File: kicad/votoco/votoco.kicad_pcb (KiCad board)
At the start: 4 copper layers, 64 x 36.5 mm, 98 parts, among them J1 Conn_01x02, J10 Conn_01x02, J11 Conn_01x02, J12 Conn_01x02, J13 Conn_01x02, J14 Conn_01x02, J2 Conn_01x04, J3 Conn_02x05_Odd_Even, J4 Conn_01x03, J5 Conn_01x02, J6 Conn_01x02, J7 Conn_01x02, J8 Conn_01x03, J9 USB_B_Micro, Q1 RQ6E045TN, Q2 RQ6E045TN, Q3 RQ6E045TN, SW1 Reset, SW2 Boot, U1 SN65HVD231, U2 TMC2209-LA-T, U3 STM32F042G6Ux, U4 74AHC1G08, U5 MAX2040xAFL, U6 NCP1117-3.3, U7 ADXL345BCCZ, Y1 12Mhz

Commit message: some error from V1.0 corrected
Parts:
- added R23: 20k, Resistor_SMD:R_0603_1608Metric, B.Cu at (133.9, 85.1)
- C16: value 10µ 50V -> 100µ 35V; footprint Capacitor_SMD:CP_Elec_4x3 -> Capacitor_SMD:CP_Elec_6.3x7.7
- U2: value TMC2209-LA-T -> QFN28_5X5_3X8_EPAD_TRI
- moved C16 6.21 mm to (139.8, 85.5), turned to 180 degrees
- moved R10 5.25 mm to (133.9, 88.2), turned to 90 degrees
- moved R9 3.51 mm to (132.2, 88.2), turned to -90 degrees
- moved C15 3.45 mm to (139.6, 89.8), turned to 180 degrees
- moved C13 0.10 mm to (142.7, 89.8)
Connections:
- R4 pad 1: GND -> +3V3
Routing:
- net GND: track 82.5 -> 88.7 mm, vias 62 -> 66
- net +24V: track 57.7 -> 62.9 mm, vias 34 -> 37
- net Net-(R10-Pad1): track 4.67 -> 6.94 mm
- net Net-(C3-Pad2): track 18.3 -> 16.1 mm
- net ENN: track 41.6 -> 43.6 mm
- net +3V3: track 42.5 -> 44.0 mm, vias 23 -> 25
- net SWCLK: track 46.6 -> 46.0 mm
- net DIR: track 24.3 -> 23.6 mm
- net SWDIO/DI2: track 86.1 -> 85.5 mm
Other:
- board text added: "Votoco 1.1"
- board text removed: "Votoco 1.0"

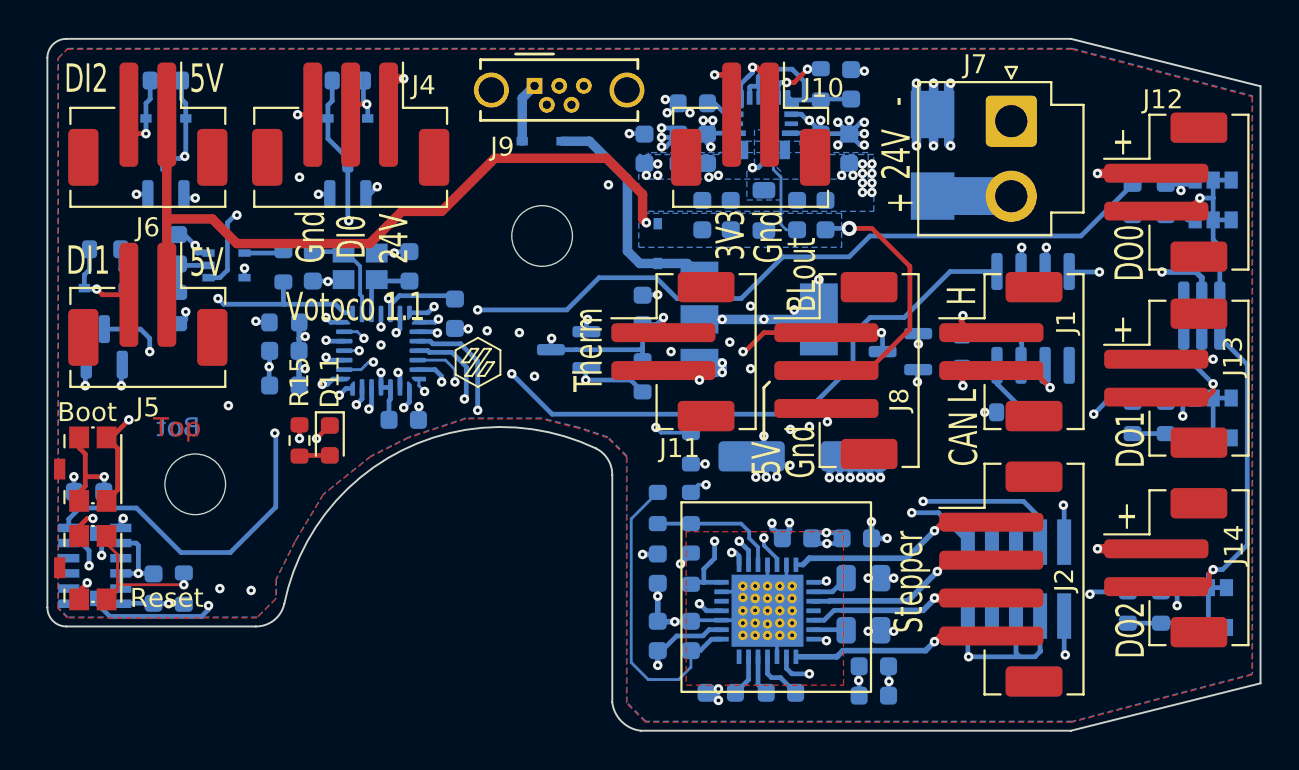
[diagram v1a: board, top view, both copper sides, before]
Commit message: temp sensor added / I2C connector added / layout almost finished
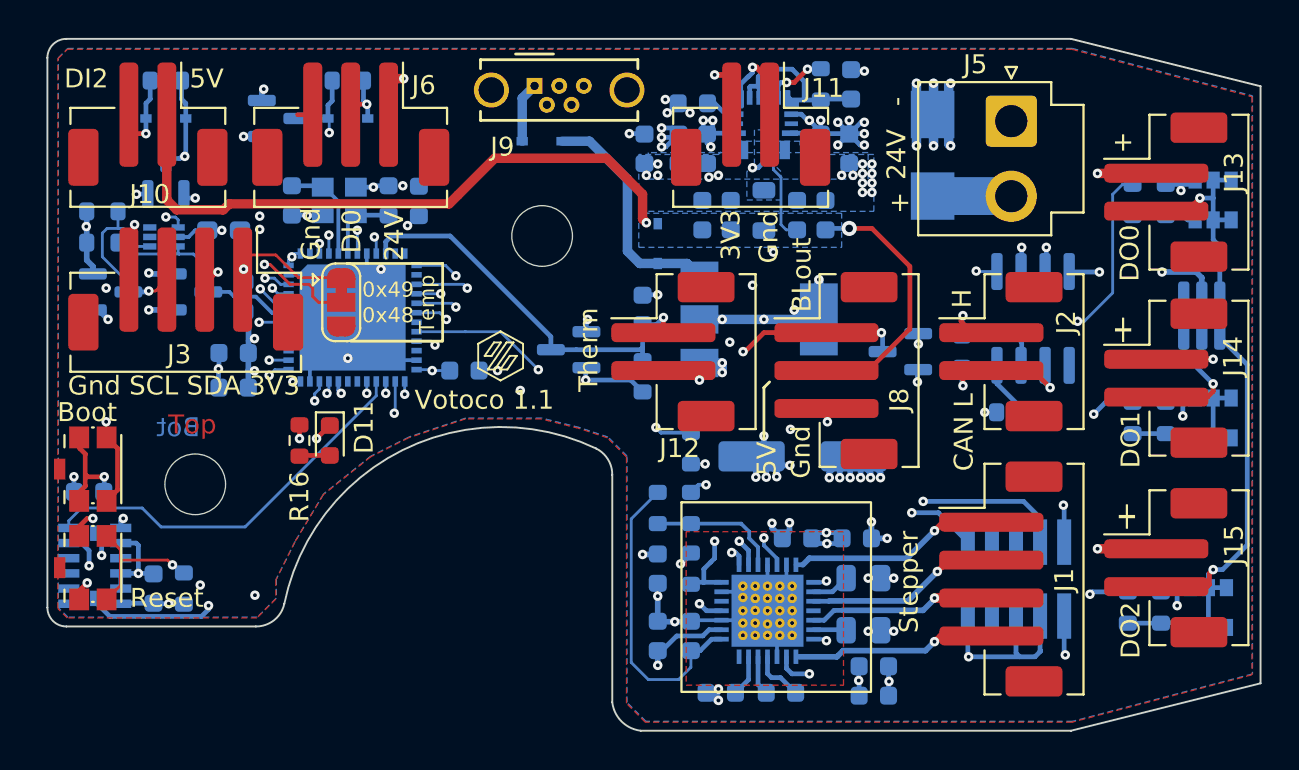
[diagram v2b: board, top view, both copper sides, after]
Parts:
- removed the C9 at (106.9, 74.6)
- removed the D3 at (103.0, 76.7)
- removed the D4 at (103.0, 79.8)
- removed the J5 at (105.3, 77.5)
- removed the R12 at (103.0, 74.6)
- removed the R3 at (112.5, 75.5)
- removed the R6 at (106.9, 77.7)
- removed the U3 at (117.6, 80.0)
- added C16: 100n, Capacitor_SMD:C_0603_1608Metric_Pad1.08x0.95mm_HandSolder, B.Cu at (109.3, 73.6)
- added D5: BAT54S, Package_TO_SOT_SMD:SOT-23, B.Cu at (103.3, 76.8)
- added D6: BAT54S, Package_TO_SOT_SMD:SOT-23, B.Cu at (107.5, 76.8)
- added J3: Conn_01x04, votoco:JST_PH_B4B-PH-SM4-TB_1x04-1MP_P2.00mm_Vertical, F.Cu at (107.3, 76.7)
- added JP1: I2C Adress Select, Jumper:SolderJumper-3_P1.3mm_Bridged12_RoundedPad1.0x1.5mm, F.Cu at (115.5, 77.4)
- added R1: 33k, Resistor_SMD:R_0603_1608Metric, B.Cu at (102.9, 72.6)
- added R2: 33k, Resistor_SMD:R_0603_1608Metric, B.Cu at (102.9, 74.2)
- added U2: STM32F072CBUx, Library:UFQFPN-48_EP_7x7_Pitch0.5mm, B.Cu at (116.1, 78.2)
- U1: renamed from U2; value QFN28_5X5_3X8_EPAD_TRI -> TMC2209-LA-T
- U4: value 74AHC1G08 -> TMP112xxDRL; footprint Package_TO_SOT_SMD:SOT-353_SC-70-5 -> Package_TO_SOT_SMD:SOT-563
- moved C12 6.25 mm to (119.6, 72.0), turned to 90 degrees
- moved D3 4.72 mm to (112.2, 67.7), turned to 0 degrees
- moved C10 4.12 mm to (122.0, 81.0)
- moved C1 3.64 mm to (112.9, 72.0)
- moved C2 3.64 mm to (118.0, 72.0)
- moved Y1 3.64 mm to (115.4, 72.0)
- moved U4 3.62 mm to (106.2, 74.0)
- moved C14 2.68 mm to (109.8, 81.9)
- moved C7 2.68 mm to (109.8, 80.1)
- moved FB1 2.50 mm to (110.4, 77.1), turned to -90 degrees
- renumbered C8 to C10, C15 to C11, C10 to C12, C16 to C13, C12 to C14, C17 to C15, C6 to C17, C26 to C25, C25 to C26, C28 to C27, C27 to C28, C11 to C6, C13 to C8, C14 to C9, D6 to D10, D7 to D2, D2 to D3, D8 to D4, D5 to D7, D9 to D8, D10 to D9, J2 to J1, J6 to J10, J10 to J11, J11 to J12, J12 to J13, J13 to J14, J14 to J15, J1 to J2, J3 to J4, J7 to J5, J4 to J6, R1 to R10, R5 to R11, R11 to R12, R13 to R14, R14 to R15, R15 to R16, R16 to R17, R17 to R18, R18 to R19, R19 to R20, R20 to R21, R21 to R22, R22 to R23, R23 to R3, R2 to R5, R7 to R6, R8 to R7, R9 to R8, R10 to R9, U1 to U3
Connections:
- D10 pad 3: SWDIO/DI2 -> DI1
- D7 pad 2: SWDIO/DI2 -> DI1
- J4 pad 2: SWDIO/DI2 -> SWDIO
- J9 pad 3: USBP/CANTX -> USBP
- R14 pad 2: SWDIO/DI2 -> DI1
- U3 pad 1: USBP/CANTX -> CANTX
- U3 pad 4: Net-(U1-Pad4) -> CANRX
- U4 pad 1: Net-(U1-Pad4) -> I2C_SCL
- U4 pad 2: Net-(C9-Pad1) -> GND
- U4 pad 3: GND -> unconnected-(U4-ALERT-Pad3)
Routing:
- net SWDIO/DI2: track 85.5 -> 0.00 mm, vias 7 -> 0
- net USBP/CANTX: track 64.5 -> 0.00 mm, vias 2 -> 0
- net Net-(U1-Pad4): track 53.9 -> 0.00 mm, vias 2 -> 0
- net CANRX: track 0.00 -> 53.8 mm, vias 0 -> 3
- net SWDIO: track 0.00 -> 47.1 mm, vias 0 -> 2
- net CANTX: track 0.00 -> 46.2 mm, vias 0 -> 3
- net USBP: track 0.00 -> 24.5 mm, vias 0 -> 1
- net I2C_SCL: track 0.00 -> 19.1 mm, vias 0 -> 2
- net I2C_SDA: track 0.00 -> 13.8 mm, vias 0 -> 1
- net DIR: track 23.6 -> 36.8 mm
- net Net-(JP1-C): track 2.10 -> 13.2 mm, vias 0 -> 2
- net +3V3: track 44.0 -> 55.1 mm
- net SPI_CS: track 32.6 -> 23.2 mm
- net DI1: track 23.9 -> 14.8 mm
- net SPI_TX: track 29.7 -> 20.9 mm, vias 2 -> 0
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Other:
- board text added: "0x48"
- board text added: "0x49"
- board text added: "CAN L"
- board text added: "Gnd SCL SDA 3V3"
- board text added: "Temp"
- board text removed: "CAN"
- board text removed: "DI1"
- board text removed: "L"

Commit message: warning clean-up
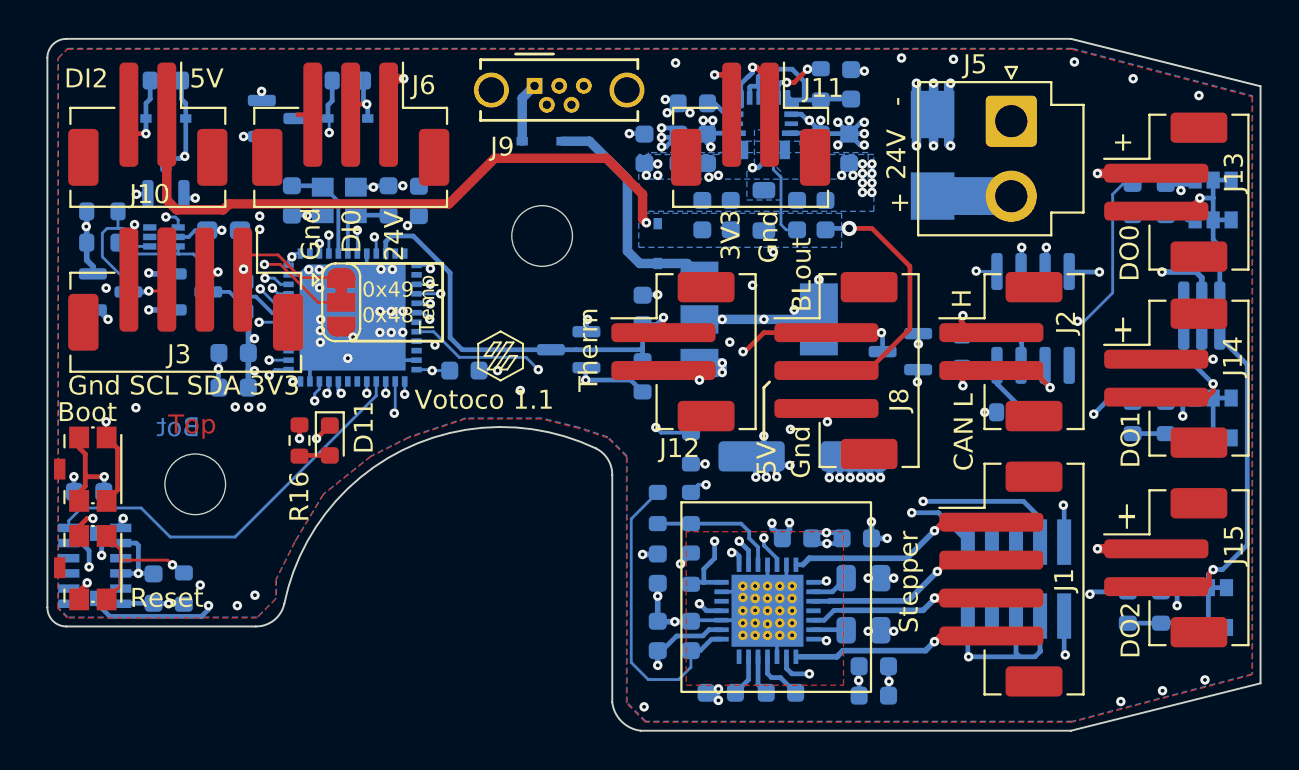
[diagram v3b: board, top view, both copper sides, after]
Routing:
- net DIR: track 36.8 -> 26.1 mm
- net AIN0: track 21.2 -> 22.8 mm
- net BLOUT: track 35.2 -> 36.2 mm
- net CANRX: track 53.8 -> 54.7 mm
- net I2C_SCL: track 19.1 -> 19.8 mm
- net I2C_SDA: track 13.8 -> 13.0 mm
- net SWDIO: track 47.1 -> 47.7 mm
- net NRESET: track 79.1 -> 78.6 mm
- net GND: vias 66 -> 95

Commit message: warning clean-up finished
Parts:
- U1: value TMC2209-LA-T -> QFN28_5X5_3X8_EPAD_TRI
- U5: value MAX2040xAFL -> 21-100532_90-100188A_MXM
- U7: value ADXL345BCCZ -> LGA_CC-14-1_ADI
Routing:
- net GND: track 90.9 -> 88.9 mm

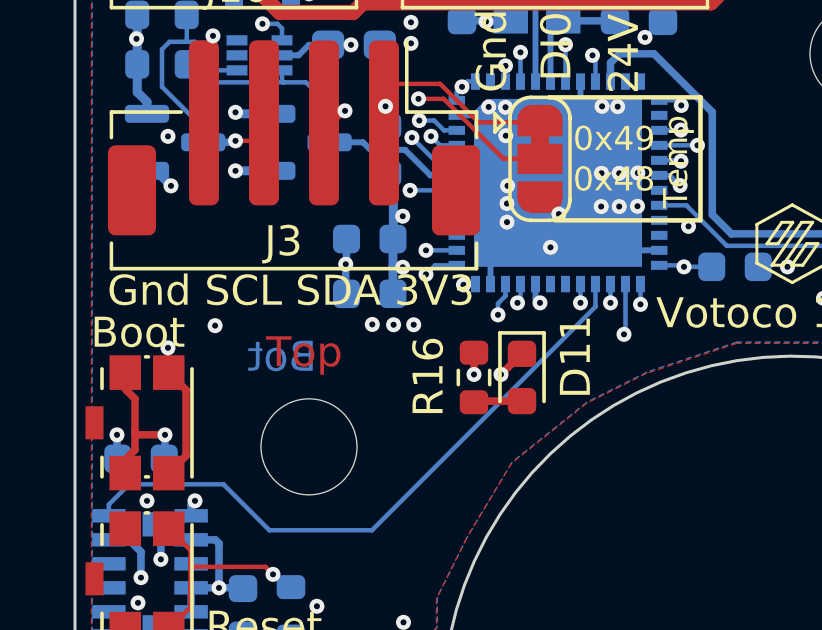
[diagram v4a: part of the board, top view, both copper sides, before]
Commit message: boot0 pull-down-added / uart-tx corrected
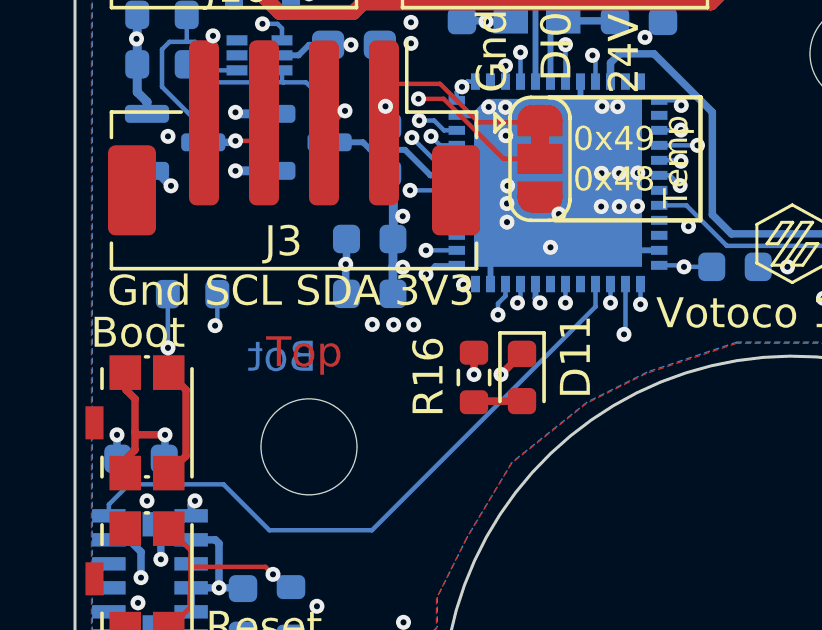
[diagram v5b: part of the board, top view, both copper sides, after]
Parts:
- added R13: 33k, Resistor_SMD:R_0603_1608Metric, B.Cu at (103.9, 81.9)
- U1: value QFN28_5X5_3X8_EPAD_TRI -> TMC2209-LA-T
- U5: value 21-100532_90-100188A_MXM -> MAX2040xAFL
- U7: value LGA_CC-14-1_ADI -> ADXL345BCCZ
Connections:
- U2 pad 29: UARTTX -> unconnected-(U2-PA8-Pad29)
- U2 pad 30: unconnected-(U2-PA9-Pad30) -> UARTTX
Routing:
- net Net-(U2-BOOT0): track 22.6 -> 24.4 mm
- net GND: track 88.9 -> 89.9 mm
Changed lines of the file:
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@@
   (net 68 "unconnected-(U1-NC-Pad25)")
   (net 69 "unconnected-(U2-PC13-Pad2)")
-  (net 70 "unconnected-(U2-PA9-Pad30)")
+  (net 70 "unconnected-(U2-PA8-Pad29)")
   (net 71 "unconnected-(U2-PA10-Pad31)")
   (net 72 "unconnected-(U2-PB4-Pad40)")
@@
   )
   (footprint "Resistor_SMD:R_0603_1608Metric" (layer "B.Cu")
+    (at 103.92 81.91)
+    (descr "Resistor SMD 0603 (1608 Metric), square (rectangular) end terminal, IPC_7351 nominal, (Body size source: IPC-SM-782 page 72, https://www.pcb-3d.com/wordpress/wp-content/uploads/ipc-sm-782a_amendment_1_and_2.pdf), generated with kicad-footprint-generator")
+    (tags "resistor")
+    (property "Sheetfile" "votoco.kicad_sch")
+    (property "Sheetname" "")
+    (property "ki_description" "Resistor")
+    (property "ki_keywords" "R res resistor")
+    (attr smd)
+    (fp_text reference "R13" (at 0 1.43) (layer "B.SilkS")
+        (effects (font (size 1 1) (thickness 0.15)) (justify mirror))
+    )
+    (fp_text value "33k" (at 0 -1.43) (layer "B.Fab")
+        (effects (font (size 1 1) (thickness 0.15)) (justify mirror))
+    )
+    (fp_text user "${REFERENCE}" (at 0 0) (layer "B.Fab")
+        (effects (font (size 0.4 0.4) (thickness 0.06)) (justify mirror))
+    )
+    (fp_line (start -0.237258 -0.5225) (end 0.237258 -0.5225)
+      (stroke (width 0.12) (type solid)) (layer "B.SilkS"))
+    (fp_line (start -0.237258 0.5225) (end 0.237258 0.5225)
+      (stroke (width 0.12) (type solid)) (layer "B.SilkS"))
+    (fp_line (start -1.48 -0.73) (end -1.48 0.73)
+      (stroke (width 0.05) (type solid)) (layer "B.CrtYd"))
+    (fp_line (start -1.48 0.73) (end 1.48 0.73)
+      (stroke (width 0.05) (type solid)) (layer "B.CrtYd"))
+    (fp_line (start 1.48 -0.73) (end -1.48 -0.73)
+      (stroke (width 0.05) (type solid)) (layer "B.CrtYd"))
+    (fp_line (start 1.48 0.73) (end 1.48 -0.73)
+      (stroke (width 0.05) (type solid)) (layer "B.CrtYd"))
+    (fp_line (start -0.8 -0.4125) (end -0.8 0.4125)
+      (stroke (width 0.1) (type solid)) (layer "B.Fab"))
+    (fp_line (start -0.8 0.4125) (end 0.8 0.4125)
+      (stroke (width 0.1) (type solid)) (layer "B.Fab"))
+    (fp_line (start 0.8 -0.4125) (end -0.8 -0.4125)
+      (stroke (width 0.1) (type solid)) (layer "B.Fab"))
+    (fp_line (start 0.8 0.4125) (end 0.8 -0.4125)
+      (stroke (width 0.1) (type solid)) (layer "B.Fab"))
+    (pad "1" smd roundrect (at -0.825 0) (size 0.8 0.95) (layers "B.Cu" "B.Paste" "B.Mask") (roundrect_rratio 0.25)
+      (net 65 "Net-(U2-BOOT0)") (pintype "passive"))
+    (pad "2" smd roundrect (at 0.825 0) (size 0.8 0.95) (layers "B.Cu" "B.Paste" "B.Mask") (roundrect_rratio 0.25)
+      (net 1 "GND") (pintype "passive"))
+    (model "${KICAD6_3DMODEL_DIR}/Resistor_SMD.3dshapes/R_0603_1608Metric.wrl"
+      (offset (xyz 0 0 0))
+      (scale (xyz 1 1 1))
+      (rotate (xyz 0 0 0))
+    )
+  )
+  (footprint "Resistor_SMD:R_0603_1608Metric" (layer "B.Cu")
     (at 106.25 65.7)
     (descr "Resistor SMD 0603 (1608 Metric), square (rectangular) end terminal, IPC_7351 nominal, (Body size source: IPC-SM-782 page 72, https://www.pcb-3d.com/wordpress/wp-content/uploads/ipc-sm-782a_amendment_1_and_2.pdf), generated with kicad-footprint-generator")
@@
         (effects (font (size 1 1) (thickness 0.15)) (justify mirror))
     )
-    (fp_text value "LGA_CC-14-1_ADI" (at 0 0) (layer "B.SilkS") hide
+    (fp_text value "ADXL345BCCZ" (at 0 0) (layer "B.SilkS") hide
         (effects (font (size 1 1) (thickness 0.15)) (justify mirror))
     )
@@
       (net 37 "SPI_TX") (pinfunction "PB15") (pintype "bidirectional") (thermal_bridge_angle 45))
     (pad "29" smd rect (at 3.375 -0.75 180) (size 0.3 0.55) (layers "B.Cu" "B.Paste" "B.Mask")
-      (net 31 "UARTTX") (pinfunction "PA8") (pintype "bidirectional") (thermal_bridge_angle 45))
+      (net 70 "unconnected-(U2-PA8-Pad29)") (pinfunction "PA8") (pintype "bidirectional") (thermal_bridge_angle 45))
     (pad "30" smd rect (at 3.375 -0.25 180) (size 0.3 0.55) (layers "B.Cu" "B.Paste" "B.Mask")
-      (net 70 "unconnected-(U2-PA9-Pad30)") (pinfunction "PA9") (pintype "bidirectional") (thermal_bridge_angle 45))
+      (net 31 "UARTTX") (pinfunction "PA9") (pintype "bidirectional") (thermal_bridge_angle 45))
     (pad "31" smd rect (at 3.375 0.25 180) (size 0.3 0.55) (layers "B.Cu" "B.Paste" "B.Mask")
       (net 71 "unconnected-(U2-PA10-Pad31)") (pinfunction "PA10") (pintype "bidirectional") (thermal_bridge_angle 45))
@@
         (effects (font (size 1 1) (thickness 0.15)) (justify mirror))
     )
-    (fp_text value "21-100532_90-100188A_MXM" (at -3.4 5.35) (layer "B.SilkS") hide
+    (fp_text value "MAX2040xAFL" (at -3.4 5.35) (layer "B.SilkS") hide
         (effects (font (size 1 1) (thickness 0.15)) (justify mirror))
     )
@@
         (effects (font (size 1 1) (thickness 0.15)) (justify mirror))
     )
-    (fp_text value "QFN28_5X5_3X8_EPAD_TRI" (at 0 0 90) (layer "Eco1.User") hide
+    (fp_text value "TMC2209-LA-T" (at 0 0 90) (layer "Eco1.User") hide
         (effects (font (size 1 1) (thickness 0.15)))
     )
@@
   (segment (start 137.2 65.276741) (end 137.2 65) (width 0.25) (layer "B.Cu") (net 1))
   (segment (start 135.6 80.6) (end 135.6 81.1) (width 0.5) (layer "B.Cu") (net 1))
+  (segment (start 104.745 82.885) (end 104.67 82.96) (width 0.15) (layer "B.Cu") (net 1))
   (segment (start 159 82.675) (end 159.875 82.675) (width 0.25) (layer "B.Cu") (net 1))
   (segment (start 135.5643 92.669999) (end 136.189999 92.669999) (width 0.2) (layer "B.Cu") (net 1))
@@
   (segment (start 144.65 94.75) (end 144.0125 94.75) (width 0.25) (layer "B.Cu") (net 1))
   (segment (start 109.05 80.8875) (end 109.025 80.9125) (width 0.25) (layer "B.Cu") (net 1))
+  (segment (start 104.745 81.91) (end 104.745 82.885) (width 0.15) (layer "B.Cu") (net 1))
   (segment (start 139.175 86) (end 137.625 86) (width 0.3) (layer "B.Cu") (net 1))
   (segment (start 137.925 86.625) (end 137.925 86.3) (width 0.3) (layer "B.Cu") (net 1))
@@
   (segment (start 150.84 71.7925) (end 150.85 71.8025) (width 1) (layer "B.Cu") (net 30))
   (segment (start 146.7 71.7925) (end 150.84 71.7925) (width 2) (layer "B.Cu") (net 30))
-  (via (at 116.85 82.2) (size 0.5) (drill 0.2) (layers "F.Cu" "B.Cu") (net 31))
+  (via (at 116.35 82.2) (size 0.5) (drill 0.2) (layers "F.Cu" "B.Cu") (net 31))
   (via (at 124.95 82.05) (size 0.5) (drill 0.2) (layers "F.Cu" "B.Cu") (net 31))
   (via (at 135.2 90) (size 0.5) (drill 0.2) (layers "F.Cu" "B.Cu") (net 31))
@@
   (segment (start 124.95 82.05) (end 125.7 82.8) (width 0.15) (layer "In1.Cu") (net 31))
   (segment (start 119.76 82.7) (end 120.41 82.05) (width 0.15) (layer "In2.Cu") (net 31))
+  (segment (start 116.7 82.2) (end 117.2 82.7) (width 0.15) (layer "In2.Cu") (net 31))
   (segment (start 117.2 82.7) (end 119.76 82.7) (width 0.15) (layer "In2.Cu") (net 31))
-  (segment (start 116.85 82.35) (end 117.2 82.7) (width 0.15) (layer "In2.Cu") (net 31))
-  (segment (start 116.85 82.2) (end 116.85 82.35) (width 0.15) (layer "In2.Cu") (net 31))
+  (segment (start 116.35 82.2) (end 116.7 82.2) (width 0.15) (layer "In2.Cu") (net 31))
   (segment (start 120.41 82.05) (end 124.95 82.05) (width 0.15) (layer "In2.Cu") (net 31))
   (segment (start 135 91.1) (end 135.2 90.9) (width 0.25) (layer "B.Cu") (net 31))
+  (segment (start 116.35 82.2) (end 116.35 81.575) (width 0.15) (layer "B.Cu") (net 31))
   (segment (start 134.63 91.47) (end 135 91.1) (width 0.25) (layer "B.Cu") (net 31))
   (segment (start 135.2 90.9) (end 135.2 90) (width 0.25) (layer "B.Cu") (net 31))
   (segment (start 134.63 92.17) (end 134.63 91.47) (width 0.25) (layer "B.Cu") (net 31))
   (segment (start 134.055 92.17) (end 133.95 92.275) (width 0.25) (layer "B.Cu") (net 31))
-  (segment (start 116.85 81.575) (end 116.85 82.2) (width 0.15) (layer "B.Cu") (net 31))
   (segment (start 135.5643 92.17) (end 134.63 92.17) (width 0.25) (layer "B.Cu") (net 31))
   (segment (start 134.63 92.17) (end 134.055 92.17) (width 0.25) (layer "B.Cu") (net 31))
@@
   (segment (start 103.455 76.295) (end 103.1 76.65) (width 0.15) (layer "In2.Cu") (net 65))
   (segment (start 110.834375 76.295) (end 103.455 76.295) (width 0.15) (layer "In2.Cu") (net 65))
+  (segment (start 103.095 81.91) (end 103.095 83.695) (width 0.15) (layer "B.Cu") (net 65))
   (segment (start 112.725 77.45) (end 111.989375 77.45) (width 0.15) (layer "B.Cu") (net 65))
+  (segment (start 103.095 83.695) (end 103.1 83.7) (width 0.15) (layer "B.Cu") (net 65))
   (segment (start 111.989375 77.45) (end 111.23016 76.690785) (width 0.15) (layer "B.Cu") (net 65))
   (via (at 111.2 72.85) (size 0.5) (drill 0.2) (layers "F.Cu" "B.Cu") (net 74))

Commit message: footprint corrected / DIR - SPI clk pins exchanged
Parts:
- C16: footprint Capacitor_SMD:C_0603_1608Metric_Pad1.08x0.95mm_HandSolder -> Capacitor_SMD:C_0603_1608Metric
- L1: value L -> 1.5µ
- U5: value MAX2040xAFL -> MAX2040xAFLA
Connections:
- U2 pad 21: SPI_CLK -> DIR
- U2 pad 26: DIR -> SPI_CLK
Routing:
- net SPI_CLK: track 29.8 -> 25.1 mm
- net DIR: track 26.1 -> 25.5 mm
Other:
- board text added: "DI1"
- board text added: "Votoco 1.2"
- board text removed: "DI2"
- board text removed: "Votoco 1.1"
